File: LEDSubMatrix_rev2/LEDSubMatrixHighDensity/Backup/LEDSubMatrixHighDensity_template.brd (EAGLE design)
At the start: 16.9 x 146 mm, 138 parts, among them IC1 TLC5955DCAR, IC2 TLC5955DCAR, IC3 TLC5955DCAR, IC4 TLC5955DCAR, IC5 TLC5955DCAR, IC6 TLC5955DCAR, IC7 TLC5955DCAR, IC8 TLC5955DCAR

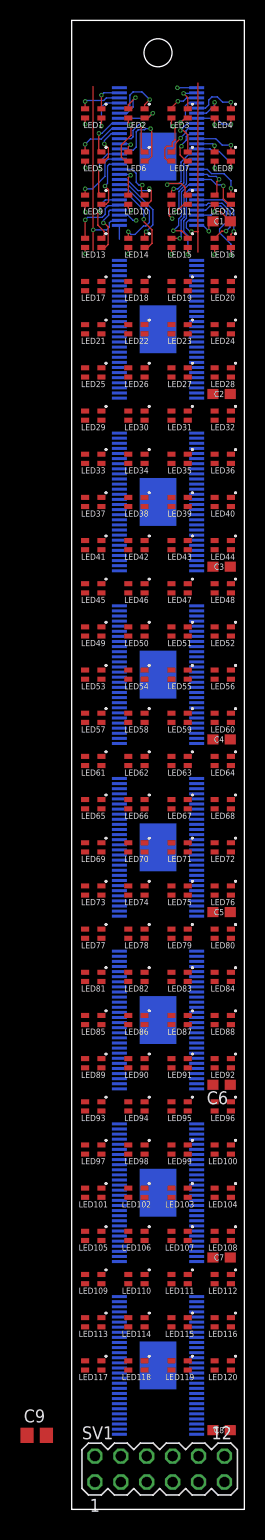
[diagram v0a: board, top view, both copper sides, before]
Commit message: Updated pinouts to align with control board
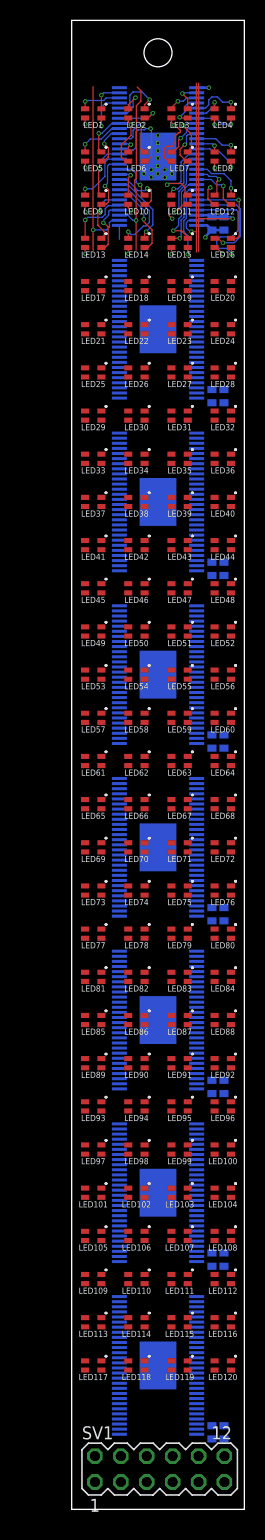
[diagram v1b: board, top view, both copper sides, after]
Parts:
- removed C9: 20uF, rcl:C0805
- added C1B, C2B, C3B, C4B, C5B, C6B, C7B, C8B: 10uF, rcl:C0402
- C1, C2, C3, C4, C5, C6, C7, C8: value 20uF -> .1uF; device rcl:C0603 -> rcl:C0402
- moved C6 0.97 mm to (13.8, -104.6), flipped to the bottom, turned to 270 degrees
- moved C7 0.97 mm to (13.8, -121.5), flipped to the bottom, turned to 270 degrees
- moved C8 0.97 mm to (13.8, -138.4), flipped to the bottom, turned to 270 degrees
- moved C1 0.97 mm to (13.8, -19.9), flipped to the bottom, turned to 270 degrees
- moved C2 0.97 mm to (13.8, -36.8), flipped to the bottom, turned to 270 degrees
- moved C3 0.97 mm to (13.8, -53.8), flipped to the bottom, turned to 270 degrees
- moved C4 0.97 mm to (13.8, -70.7), flipped to the bottom, turned to 270 degrees
- moved C5 0.97 mm to (13.8, -87.6), flipped to the bottom, turned to 270 degrees
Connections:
- new net 3V3_LOGIC: C1.1, C1B.1, C2.1, C2B.1, C3.1, C3B.1, C4.1, C4B.1, C5.1, C5B.1, C6.1, C6B.1, C7.1, C7B.1, C8.1, C8B.1, IC1.54, IC2.54, IC3.54, IC4.54, IC5.54, IC6.54, IC7.54, IC8.54, SV1.9
- net 3V3: no longer C1.1, C2.1, C3.1, C4.1, C5.1, C6.1, C7.1, C8.1, C9.1, IC1.54, IC2.54, IC3.54, IC4.54, IC5.54, IC6.54, IC7.54, IC8.54
- net GND: now also C1B.2, C2B.2, C3B.2, C4B.2, C5B.2, C6B.2, C7B.2, C8B.2; no longer C9.2, SV1.9
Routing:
- net 3V3_LOGIC: track 0.00 -> 23.5 mm, vias 0 -> 1
- net LAT: track 1.85 -> 18.3 mm
- net N$LEDR16: track 7.20 -> 10.1 mm
- net N$LEDB16: track 8.98 -> 11.6 mm
- net N$LEDG16: track 6.91 -> 8.57 mm
- net 3V3: track 23.5 -> 22.0 mm
- net GND: track 4.46 -> 5.06 mm, vias 2 -> 14
- net N$LEDB3: track 3.98 -> 3.41 mm
